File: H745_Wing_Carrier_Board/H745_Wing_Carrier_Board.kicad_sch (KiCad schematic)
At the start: 7 parts

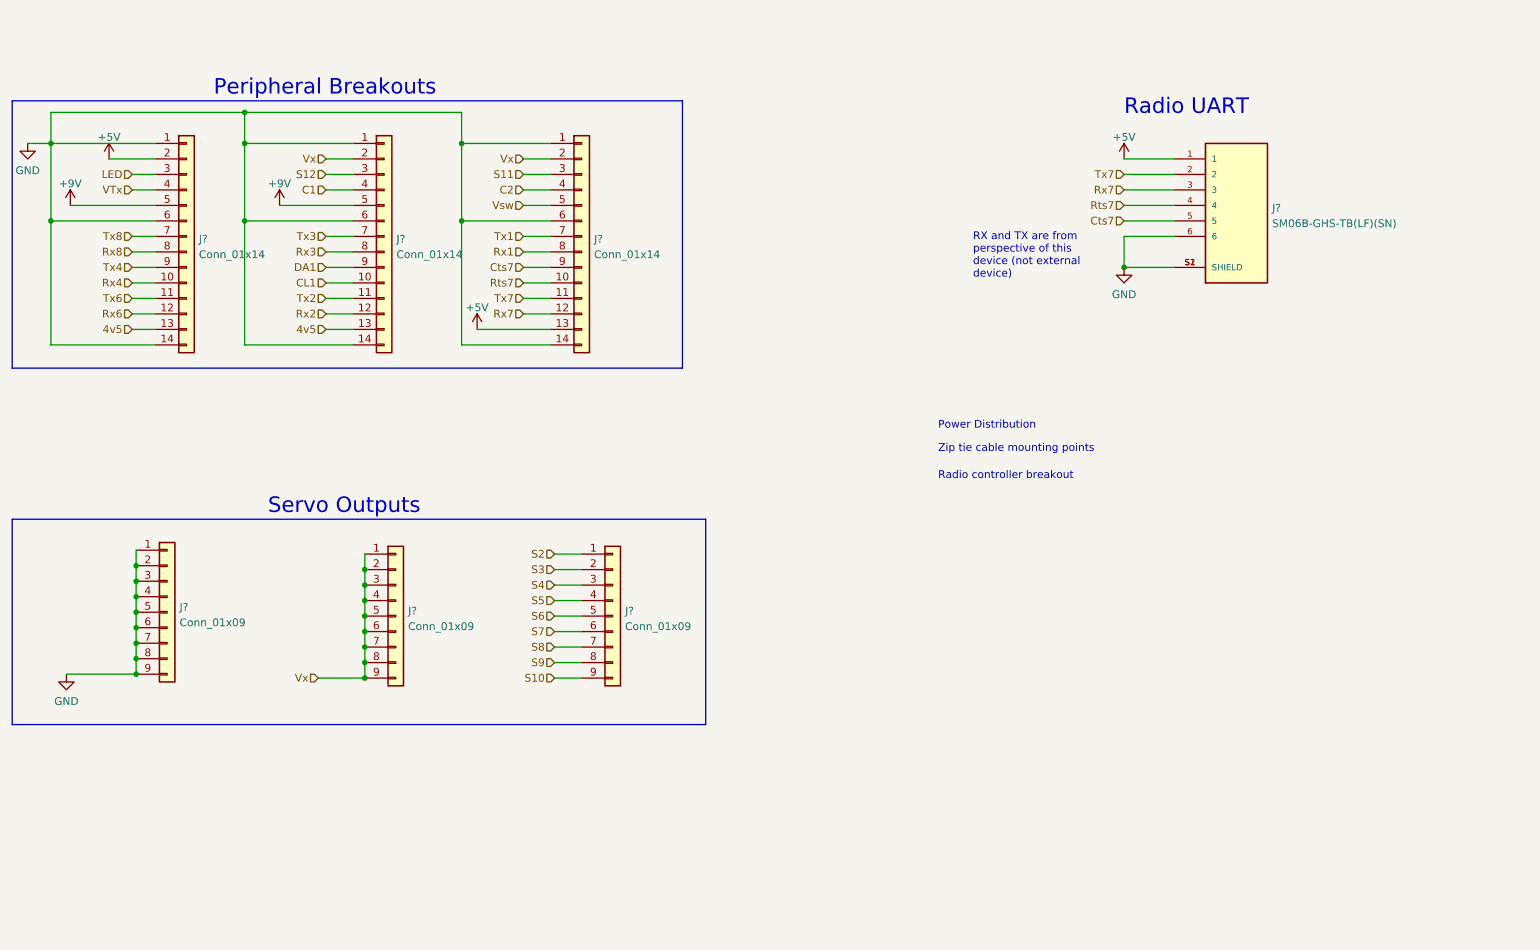
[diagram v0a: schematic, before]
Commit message: Added RFD900ux library
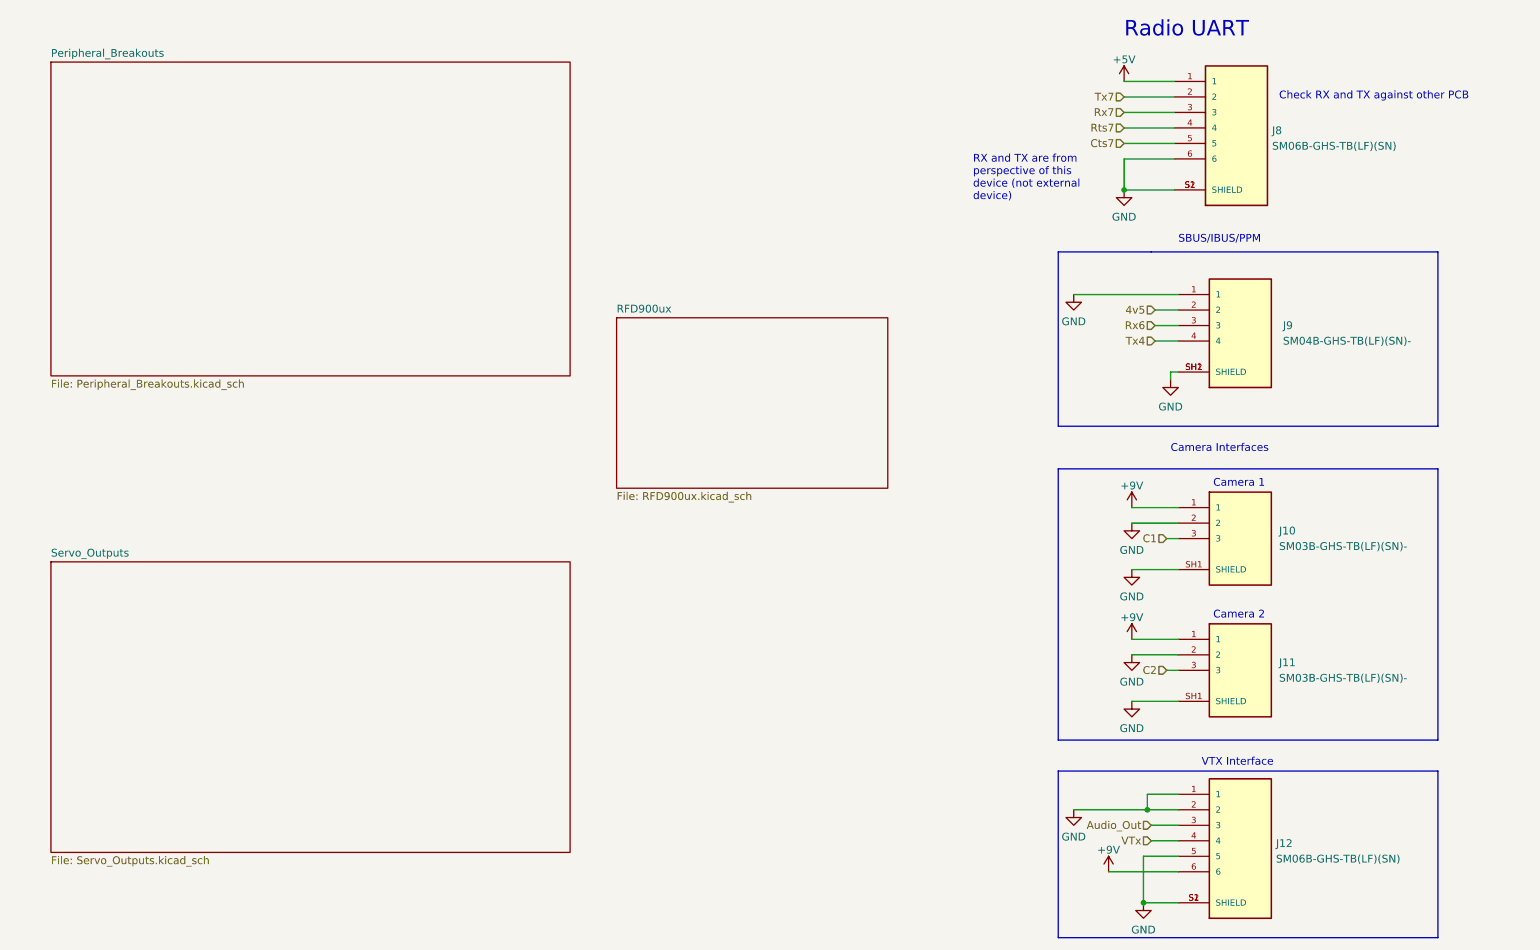
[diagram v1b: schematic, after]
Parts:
- removed J? (x3): Conn_01x14, symbol Connector_Generic:Conn_01x14
- removed J? (x3): Conn_01x09, symbol Connector_Generic:Conn_01x09
- added J10, J11: SM03B-GHS-TB(LF)(SN)-, Footprints:JST_SM03B-GHS-TB(LF)(SN)-, symbol SM03B-GHS-TB_LF__SN_:SM03B-GHS-TB(LF)(SN)-
- added J12: SM06B-GHS-TB(LF)(SN), Footprints:JST_SM06B-GHS-TB(LF)(SN), symbol SM06B-GHS-TB_LF__SN_:SM06B-GHS-TB(LF)(SN)
- added J9: SM04B-GHS-TB(LF)(SN)-, JST_SM04B-GHS-TB(LF)(SN)-, symbol SM03B-GHS-TB_LF__SN_:SM04B-GHS-TB(LF)(SN)-
- gave numbers to parts that had none: 1
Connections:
- net +9V: now also J10.1, J11.1, J12.6
- net 4v5: now also J9.2
- net C1: now also J10.3
- net C2: now also J11.3
- net GND: now also J10.2, J10.SH1 (SHIELD), J11.2, J11.SH1 (SHIELD), J12.1, J12.2, J12.5, J12.S1 (SHIELD), J12.S2 (SHIELD), J9.1, J9.SH1 (SHIELD), J9.SH2 (SHIELD)
- net Rx6: now also J9.3
- net Tx4: now also J9.4
- net VTx: now also J12.4
- new net Audio_Out: J12.3
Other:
- added sheet Peripheral_Breakouts (Peripheral_Breakouts.kicad_sch)
- added sheet RFD900ux (RFD900ux.kicad_sch)
- added sheet Servo_Outputs (Servo_Outputs.kicad_sch)
- note added: "Camera 1"
- note added: "Camera 2"
- note added: "Camera Interfaces"
- note added: "Check RX and TX against other PCB"
- note added: "SBUS/IBUS/PPM"
- note added: "VTX Interface"
- note removed: "Peripheral Breakouts"
- note removed: "Power Distribution"
- note removed: "Radio controller breakout"
- note removed: "Servo Outputs"
- note removed: "Zip tie cable mounting points"
- moved on the sheet: J8

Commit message: Added rfd900ux
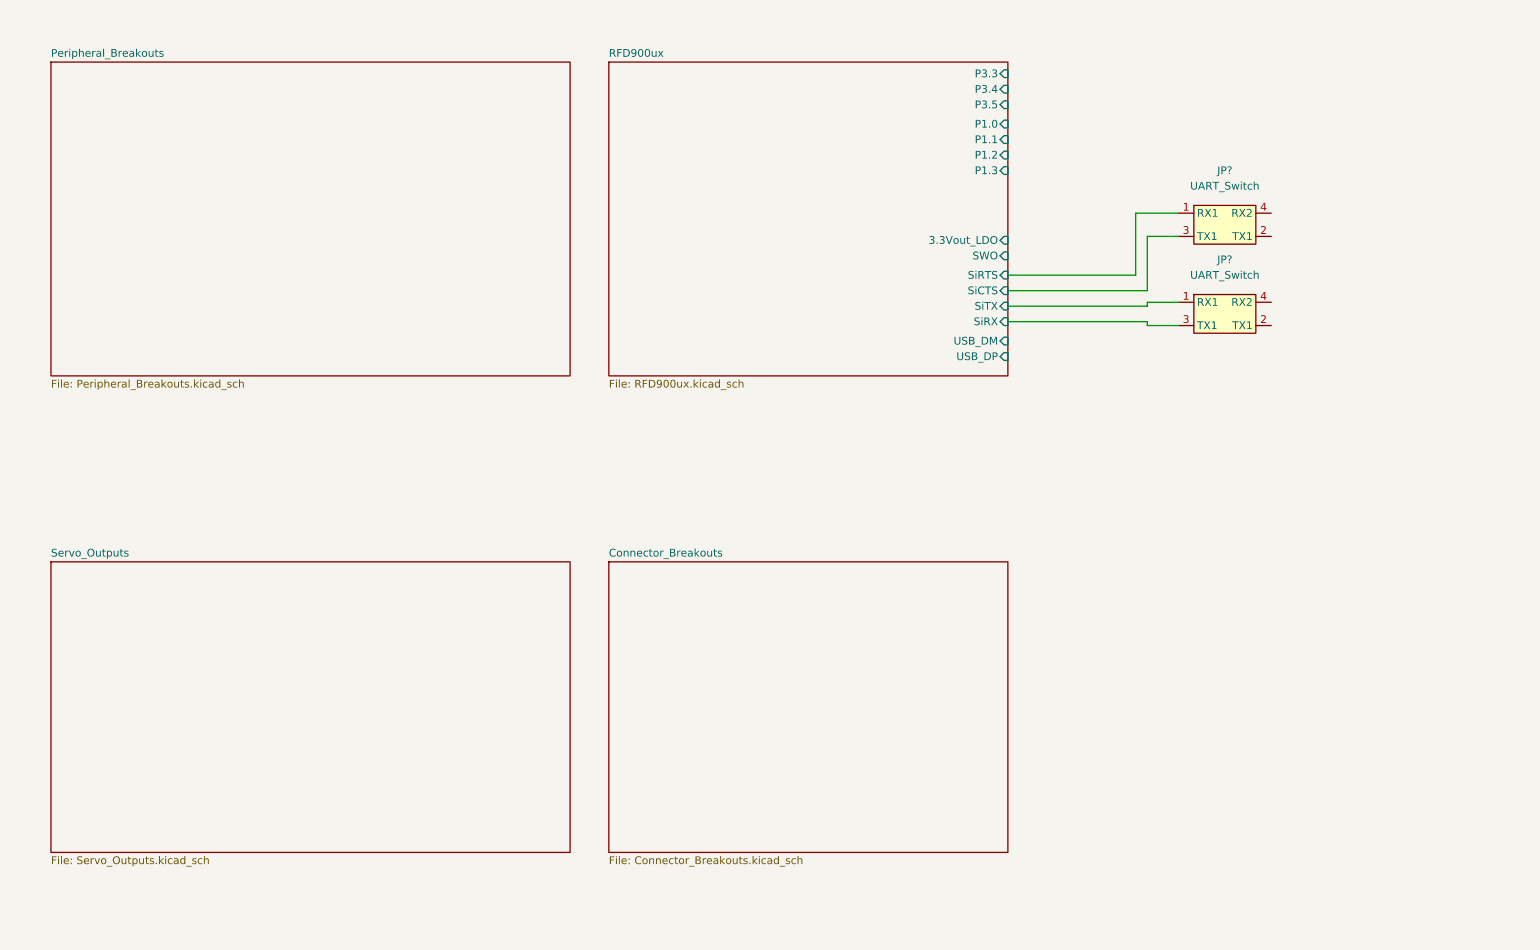
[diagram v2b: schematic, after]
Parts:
- removed J10, J11: SM03B-GHS-TB(LF)(SN)-, Footprints:JST_SM03B-GHS-TB(LF)(SN)-, symbol SM03B-GHS-TB_LF__SN_:SM03B-GHS-TB(LF)(SN)-
- removed J12, J8: SM06B-GHS-TB(LF)(SN), Footprints:JST_SM06B-GHS-TB(LF)(SN), symbol SM06B-GHS-TB_LF__SN_:SM06B-GHS-TB(LF)(SN)
- removed J9: SM04B-GHS-TB(LF)(SN)-, JST_SM04B-GHS-TB(LF)(SN)-, symbol SM03B-GHS-TB_LF__SN_:SM04B-GHS-TB(LF)(SN)-
- added JP? (x2): UART_Switch, symbol UART_Switch:UART_Switch
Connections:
- new net RFD900ux/SiCTS: JP?.3 (TX1)
- new net RFD900ux/SiRTS: JP?.1 (RX1)
- new net RFD900ux/SiRX: JP?.3 (TX1)
- new net RFD900ux/SiTX: JP?.1 (RX1)
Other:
- added sheet Connector_Breakouts (Connector_Breakouts.kicad_sch)
- sheet RFD900ux ports: added 3.3Vout_LDO, P1.0, P1.1, P1.2, P1.3, P3.3, P3.4, P3.5, SWO, SiCTS, SiRTS, SiRX, SiTX, USB_DM, USB_DP; removed none
- note removed: "Camera 1"
- note removed: "Camera 2"
- note removed: "Camera Interfaces"
- note removed: "Check RX and TX against other PCB"
- note removed: "RX and TX are from perspective of this device (not external device)"
- note removed: "Radio UART"
- note removed: "SBUS/IBUS/PPM"
- note removed: "VTX Interface"

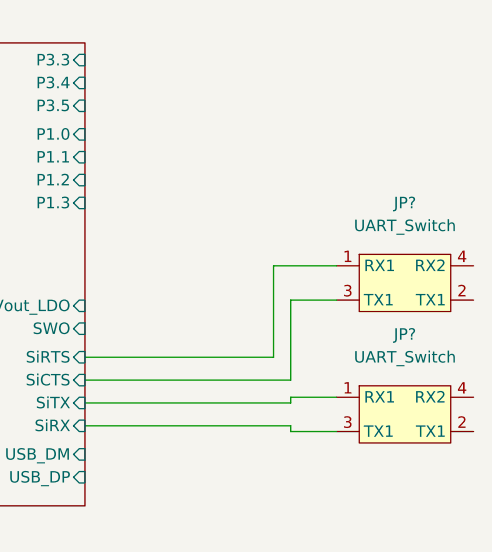
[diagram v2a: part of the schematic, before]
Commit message: Added footprints for ux
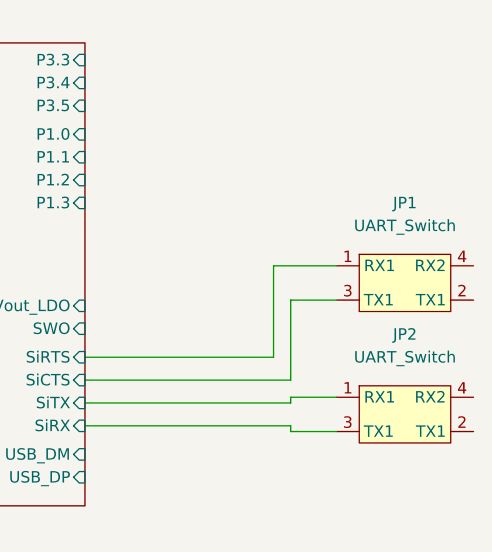
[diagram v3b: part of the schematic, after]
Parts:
- gave numbers to parts that had none: 2

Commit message: Fixed layout
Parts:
- JP1, JP2: footprint (none) -> Footprints:UART_Switch
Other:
- sheet Connector_Breakouts ports: added 4v5, Audio_Out, C1, C2, Cts7, Rts7, Rx6, Rx7, Tx4, Tx7, VTx; removed none
- sheet Peripheral_Breakouts ports: added 4v5, C1, C2, CL1, Cts7, DA1, LED, Rts7, Rx1, Rx2, Rx3, Rx4, Rx6, Rx7, Rx8, S11, S12, Tx1, Tx2, Tx3, Tx4, Tx6, Tx7, Tx8, VTx, Vsw, Vx; removed none
- sheet Servo_Outputs ports: added S1, S10, S2, S3, S4, S5, S6, S7, S8, S9, Vx; removed none

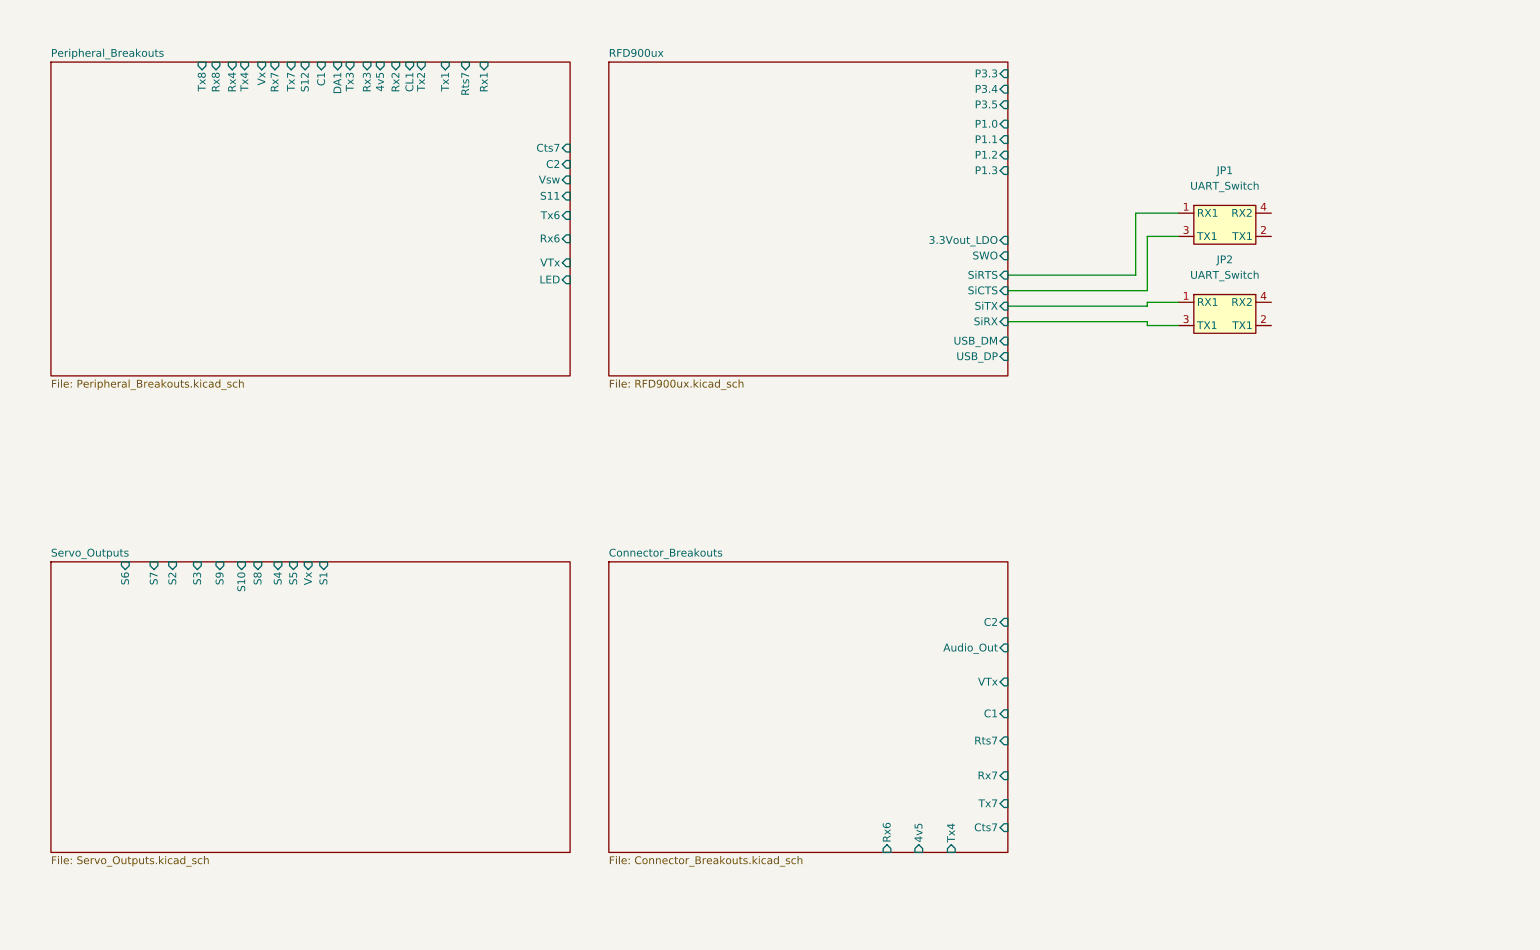
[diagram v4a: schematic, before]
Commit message: Traced together some stuff:
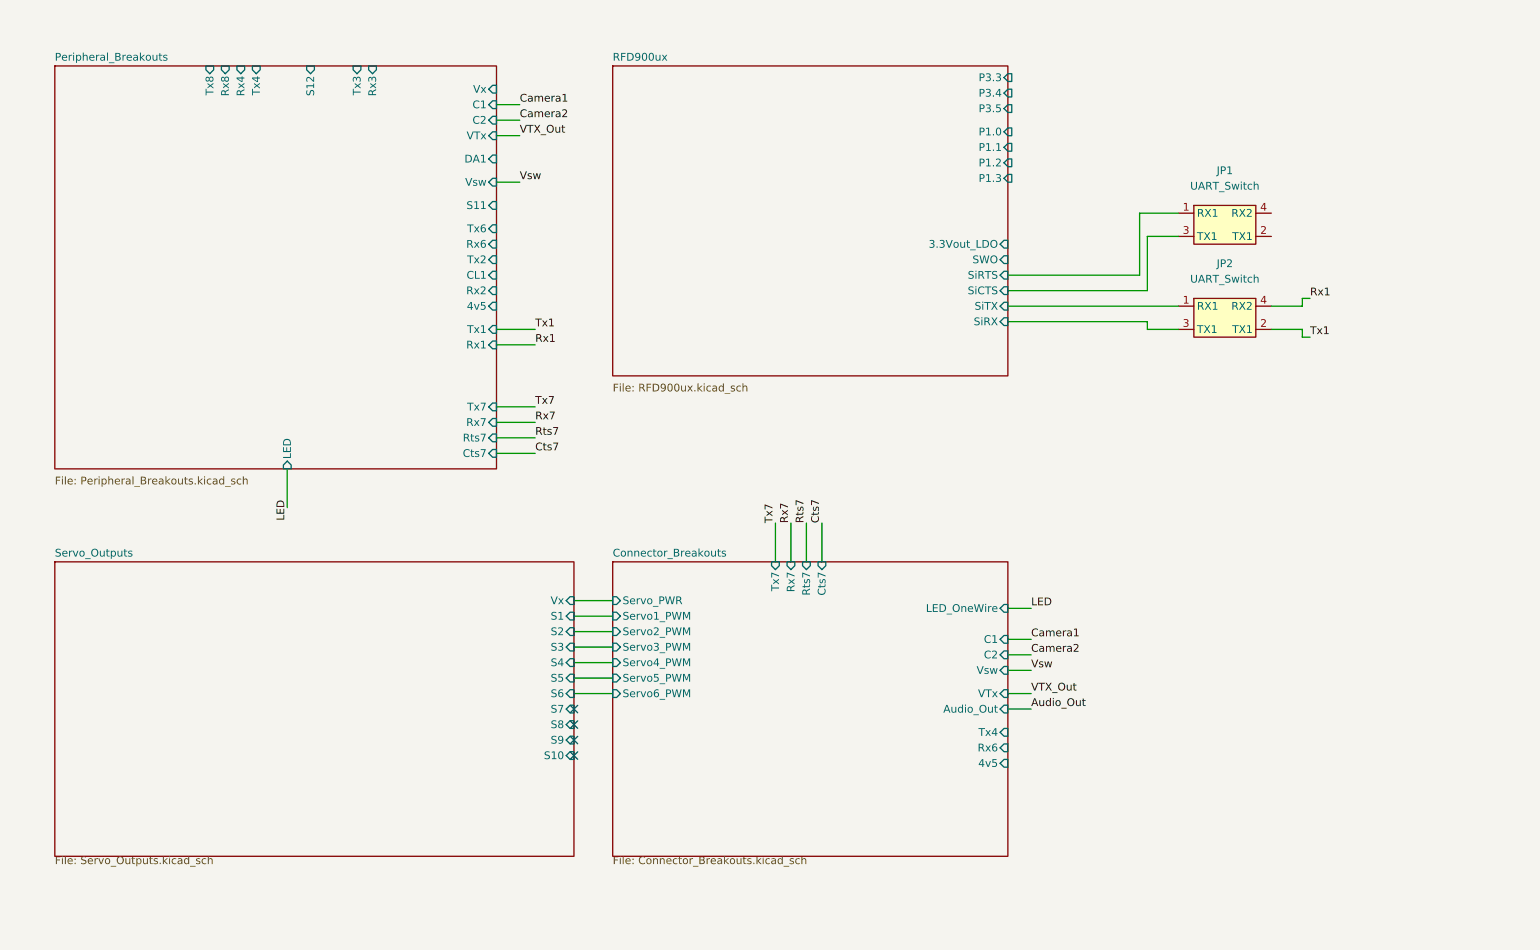
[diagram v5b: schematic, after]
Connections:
- net Tx1: now reaches JP2.2 (TX1)
- net Rx1: now reaches JP2.4 (RX2)
- no-connect marks 0 -> 4
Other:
- sheet Connector_Breakouts ports: added LED_OneWire, Servo1_PWM, Servo2_PWM, Servo3_PWM, Servo4_PWM, Servo5_PWM, Servo6_PWM, Servo_PWR, Vsw; removed none
- sheet RFD900ux ports: added none; removed USB_DM, USB_DP
- moved on the sheet: JP2
